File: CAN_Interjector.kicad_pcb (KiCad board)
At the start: 2 copper layers, 5 parts, among them J1 Conn_01x02, J2 Conn_01x02, SW1 SW_DPDT_x2

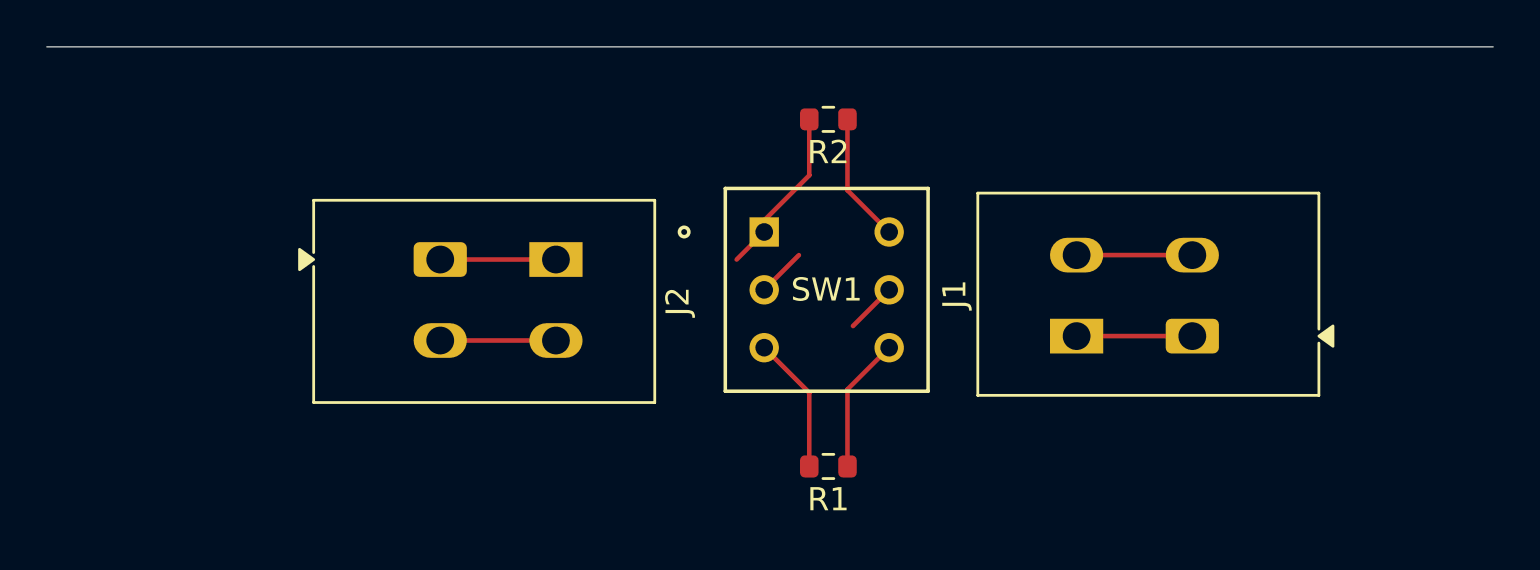
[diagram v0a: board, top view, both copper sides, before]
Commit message: Cut down board, added traces, added 3d models
Signed-off-by: cfinn <cfinn68916@proton.me>
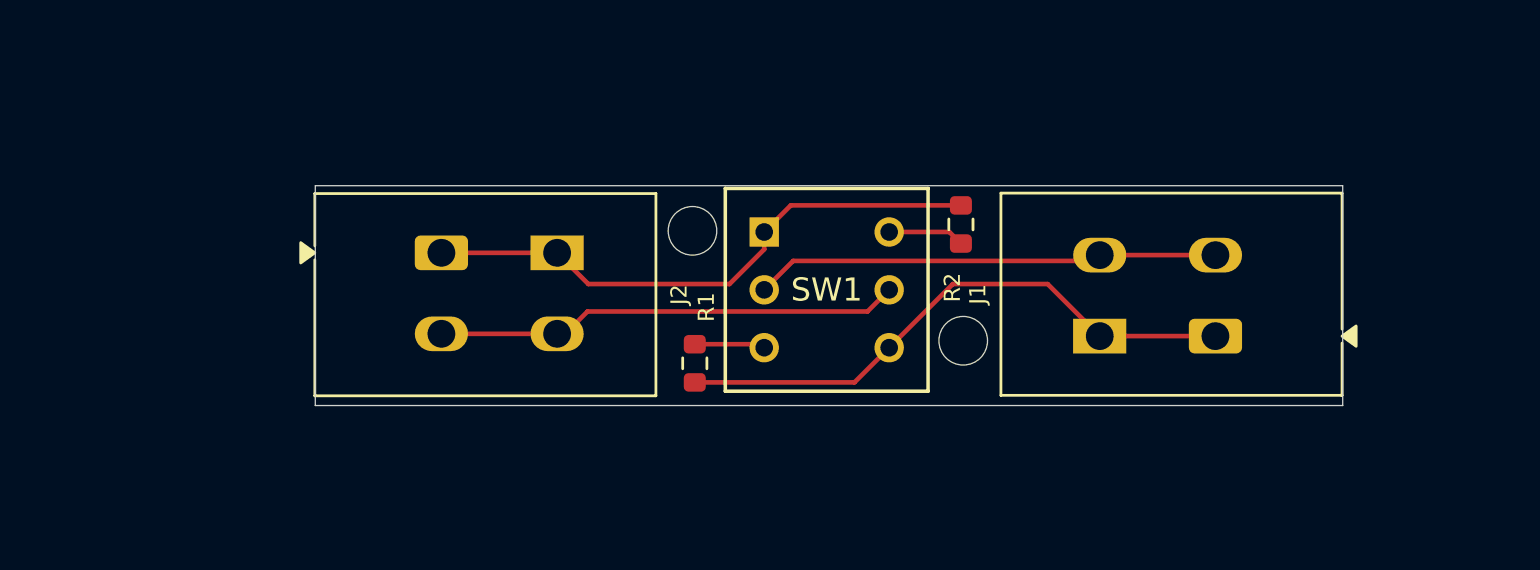
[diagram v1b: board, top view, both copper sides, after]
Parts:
- moved R2 7.31 mm to (163.5, 102.7), turned to 90 degrees
- moved R1 7.29 mm to (152.0, 108.7), turned to 90 degrees
- moved J1 1.00 mm to (174.5, 107.5)
- moved J2 0.29 mm to (141.1, 103.9)
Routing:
- net Net-(J1-Pin_1): track 12.1 -> 25.9 mm
- net Net-(J1-Pin_2): track 7.12 -> 20.5 mm
- net Net-(J2-Pin_1): track 12.4 -> 25.4 mm
- net Net-(J2-Pin_2): track 8.10 -> 20.1 mm
- net Net-(SW1A-C): track 5.94 -> 3.06 mm
- net Net-(SW1B-C): track 5.61 -> 3.31 mm
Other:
- board outline added: 44.4 x 9.5 mm
- board text added: "A"
- board text added: "B"
- board text added: "CAN Bus Interjector V0.1"
- board text added: "FRC Team 1716"
- board text added: "github.com/Brown-County-FIRST-Robotics/CAN_Interjector"
